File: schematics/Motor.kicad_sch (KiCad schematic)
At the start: 21 parts, among them Q2 MMBT3904, Q3 MMBT3904, Q34 MMBT3904, Q4 MMBT3904

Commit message: Множественные обновления схем
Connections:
- net +5V: no longer MC10.4
- new net EN: MC10.4
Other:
- company: Филимонов и К -> (none)
- title: (none) -> OctopusNode
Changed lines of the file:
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@@
 	(paper "A4")
 	(title_block
-		(company "Филимонов и К")
+		(title "OctopusNode")
 		(comment 1 "Мотор")
 		(comment 2 "Филимонов С.В.")
@@
 	)
 	(junction
-		(at 213.36 55.88)
-		(diameter 0)
-		(color 0 0 0 0)
-	)
-	(junction
-		(at 214.63 43.18)
+		(at 212.09 55.88)
 		(diameter 0)
 		(color 0 0 0 0)
@@
 	(wire
 		(pts
-			(xy 213.36 40.64) (xy 236.22 40.64)
+			(xy 212.09 40.64) (xy 236.22 40.64)
 		)
 		(stroke
@@
 	(wire
 		(pts
-			(xy 214.63 50.8) (xy 236.22 50.8)
+			(xy 218.44 50.8) (xy 236.22 50.8)
 		)
 		(stroke
@@
 	(wire
 		(pts
-			(xy 213.36 55.88) (xy 236.22 55.88)
-		)
-		(stroke
-			(width 0)
-			(type default)
-		)
-	)
-	(wire
-		(pts
 			(xy 179.07 99.06) (xy 179.07 101.6)
 		)
@@
 	(wire
 		(pts
-			(xy 214.63 50.8) (xy 214.63 43.18)
-		)
-		(stroke
-			(width 0)
-			(type default)
-		)
-	)
-	(wire
-		(pts
-			(xy 213.36 64.77) (xy 213.36 55.88)
+			(xy 212.09 64.77) (xy 212.09 55.88)
 		)
 		(stroke
@@
 	(wire
 		(pts
-			(xy 213.36 55.88) (xy 213.36 40.64)
+			(xy 212.09 55.88) (xy 212.09 40.64)
 		)
 		(stroke
@@
 	(wire
 		(pts
+			(xy 212.09 55.88) (xy 236.22 55.88)
+		)
+		(stroke
+			(width 0)
+			(type default)
+		)
+	)
+	(wire
+		(pts
 			(xy 95.25 68.58) (xy 102.87 68.58)
 		)
@@
 			"AAAAAAAAAAAAAAAAAAAAAAAAAAAAAAAAAAAAAAAAAAAAAAAAAAAAAAAAAAAAAAAAAAAAAAAAAAAA"
 			"AAAAAAAAAAAAAAAAAAAAAAAAAAAAAAAAAAAAAAAAAAAAAAAAAAAAAAAAAAAAAAAAAAAAAAAAAAAA"
-			"AAAAAAAAAAAAAAAAAAAAAAAAAA=="
+			"AAAAAAAAAAAAAAAAAAAAAAAAAAAFAAAAAAAAAAcAAAAAAACAAAAAAAAAAAAAAAAAAAAAAAQAAAAB"
+			"AAAAOQAAAG0AAABtAAAAAAAAAAAAAAAAAAADAAAAAAAAAAAAAAAAAAAAAAQAAAABAAAAoF1WCgBg"
+			"AAAGAAAAAAAAAAgAAAAAAACAAAAAAAAAAAAAAAAAAAAAAAQAAAABAAAAOQAAAG0AAABtAAAAAAAA"
+			"AAAAAAAAAAADAAAAAAAAAAAAAAAAAAAAAAQAAAABAAAA0B+9NgEAAABWAAAAAAAAAFgAAAAAAACA"
+			"AAAAAAAAAAAAAAAAAAAAAAEAAAABAAAA0Cu9NgEAAAC3AAAAAAAAALgAAAAAAACAAAAAAAAAAAAA"
+			"AAAAAAAAAAEAAAABAAAASAQAAAEAAACwLVg3AQAAAAAcAAAAAAAAEC1YNwEAAABJBAAAAQAAALAt"
+			"WDcBAAAAABwAAAAAAAAwLVg3AQAAAEoEAAABAAAAsC1YNwEAAAAAHAAAAAAAAFAtWDcBAAAATgQA"
+			"AAEAAACwLVg3AQAAAAAcAAAAAAAAcC1YNwEAAAAYAAAAAQAAADB3G18BAAAAAQAAAAAAAAA0GQAA"
+			"AQAAAMgEAAAhAAAAyAQAACcAAAAYAAAAAAAAADB3G18BAAAAAQAAAAEAAAA3BAAAAQAAAMgEAAAh"
+			"AAAAyAQAACcAAABNBAAAAQAAALAtWDcBAAAAABwAAAAAAACQLVg3AQAAAEsEAAABAAAAsC1YNwEA"
+			"AAAAHAAAAAAAABAuWDcBAAAAOAQAAAEAAACwLVg3AQAAAAAcAAAAAAAAMC5YNwEAAAA3BAAAAQAA"
+			"ALAtWDcBAAAAABwAAAEAAABQLlg3AQAAADYEAAAAAAAAsC1YNwEAAAAAHAAAAQAAAHAuWDcBAAAA"
+			"KgQAAAEAAACwLVg3AQAAAAAcAAABAAAAkC5YNwEAAAAYAAAAAQAAADB3G18BAAAAAQAAAAEAAAA4"
+			"GQAAAQAAAMgEAAAhAAAAyAQAACcAAAAAAAAAAAAAAAAAAAAAAAAA8QQAAAEAAAAAL1g3AQAAAAAc"
+			"AAABAAAAAAAAAAAAAAABAAAAAAAAALAtWDcBAAAAEQAAAAEAAADA6hQ3AQAAADAvWDcBAAAAAAAA"
+			"AAAAAADIBAAAIQAAAMgEAAAnAAAAYgQAADcAAABAL1g3AQAAAAAcAAAXAAAAsC5YNwEAAAARAAAA"
+			"AQAAAHAsWDcBAAAAMC9YNwEAAAAAAAAAAAAAAMgEAAAdAAAAyAQAACgAAAAYAAAAAQAAADDV4QoB"
+			"AAAAAQAAAAEAAAAfBQAAEwAAAMgEAAAdAAAAyAQAACAAAABNBAAAAQAAAJAvWDcBAAAAAHimSQMA"
+			"AAD5LFg3AQAAAADuXTcBAAAATQ=="
 		)
 	)
@@
 		)
 	)
+	(global_label "EN"
+		(shape input)
+		(at 218.44 50.8 180)
+		(fields_autoplaced yes)
+		(effects
+			(font
+				(size 1.27 1.27)
+			)
+			(justify right)
+		)
+		(property "Intersheetrefs" "${INTERSHEET_REFS}"
+			(at 212.9753 50.8 0)
+			(effects
+				(font
+					(size 1.27 1.27)
+				)
+				(justify right)
+				(hide yes)
+			)
+		)
+	)
 	(hierarchical_label "MOTOR_DIR"
 		(shape input)
@@
 	(symbol
 		(lib_id "power:GND")
-		(at 213.36 64.77 0)
+		(at 212.09 64.77 0)
 		(unit 1)
 		(exclude_from_sim no)
@@
 		(fields_autoplaced yes)
 		(property "Reference" "#PWR0212"
-			(at 213.36 71.12 0)
+			(at 212.09 71.12 0)
 			(effects
 				(font
@@
 		)
 		(property "Value" "GND"
-			(at 213.36 69.85 0)
+			(at 212.09 69.85 0)
 			(effects
 				(font
@@
 		)
 		(property "Footprint" ""
-			(at 213.36 64.77 0)
+			(at 212.09 64.77 0)
 			(effects
 				(font
@@
 		)
 		(property "Datasheet" ""
-			(at 213.36 64.77 0)
+			(at 212.09 64.77 0)
 			(effects
 				(font
@@
 		)
 		(property "Description" "Power symbol creates a global label with name \"GND\" , ground"
-			(at 213.36 64.77 0)
+			(at 212.09 64.77 0)
 			(effects
 				(font

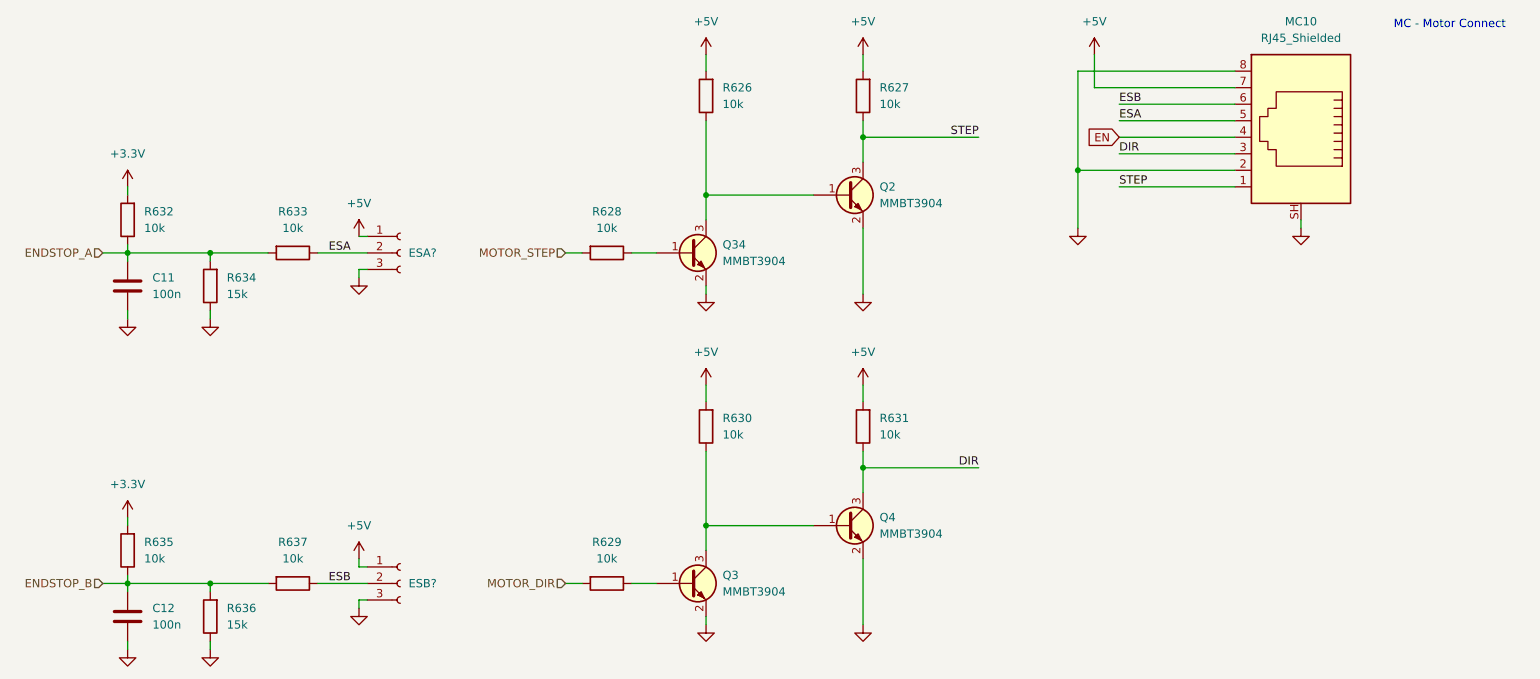
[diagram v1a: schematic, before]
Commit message: Обновил обозначения, а то старая нумерация была специфической
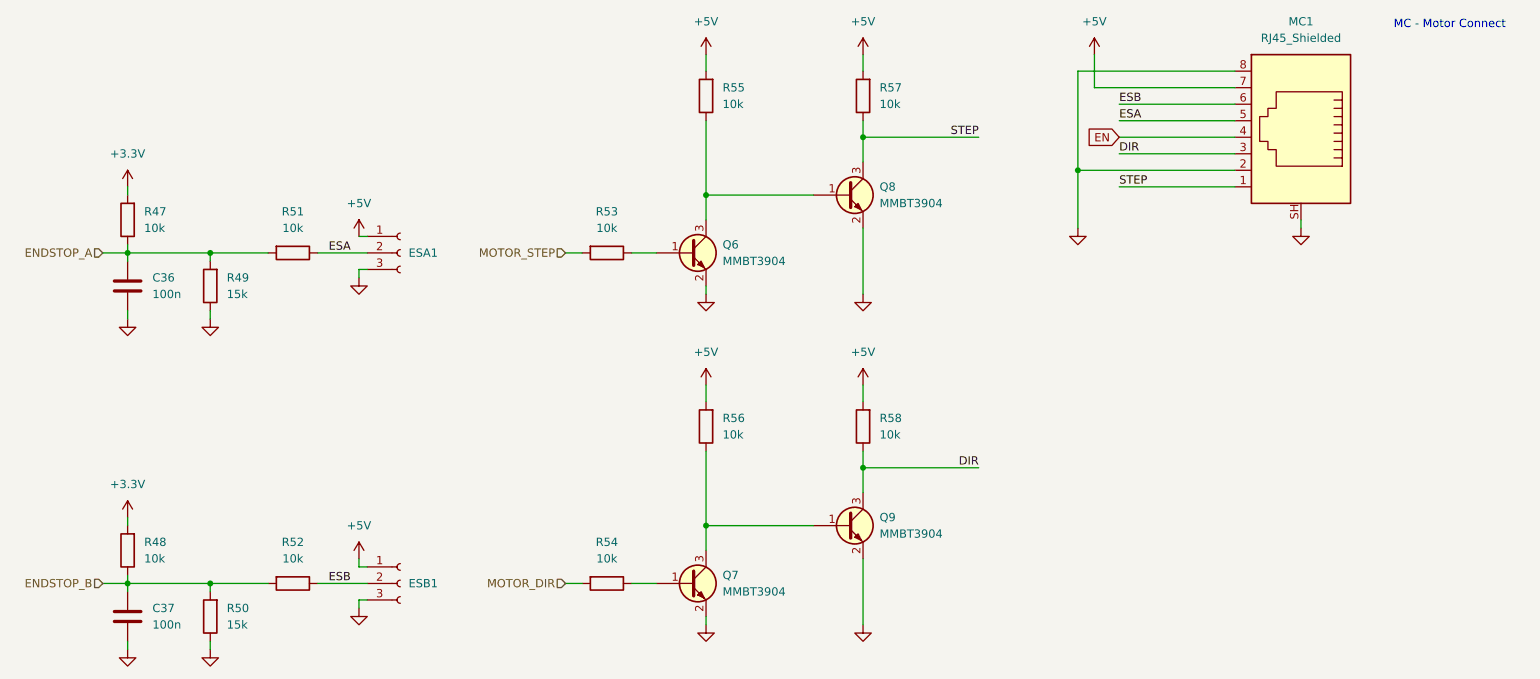
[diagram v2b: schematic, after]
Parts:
- gave numbers to parts that had none: 2
- renumbered C11 to C36, C12 to C37, MC10 to MC1, Q34 to Q6, Q3 to Q7, Q2 to Q8, Q4 to Q9, R632 to R47, R635 to R48, R634 to R49, R636 to R50, R633 to R51, R637 to R52, R628 to R53, R629 to R54, R626 to R55, R630 to R56, R627 to R57, R631 to R58
